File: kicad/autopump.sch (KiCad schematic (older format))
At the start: 12 parts, among them P1 HE10-16, P2 CONN_01X03, P3 CONN_01X06, P4 CONN_01X16, SW1 SW_PUSH, SW2 SW_PUSH

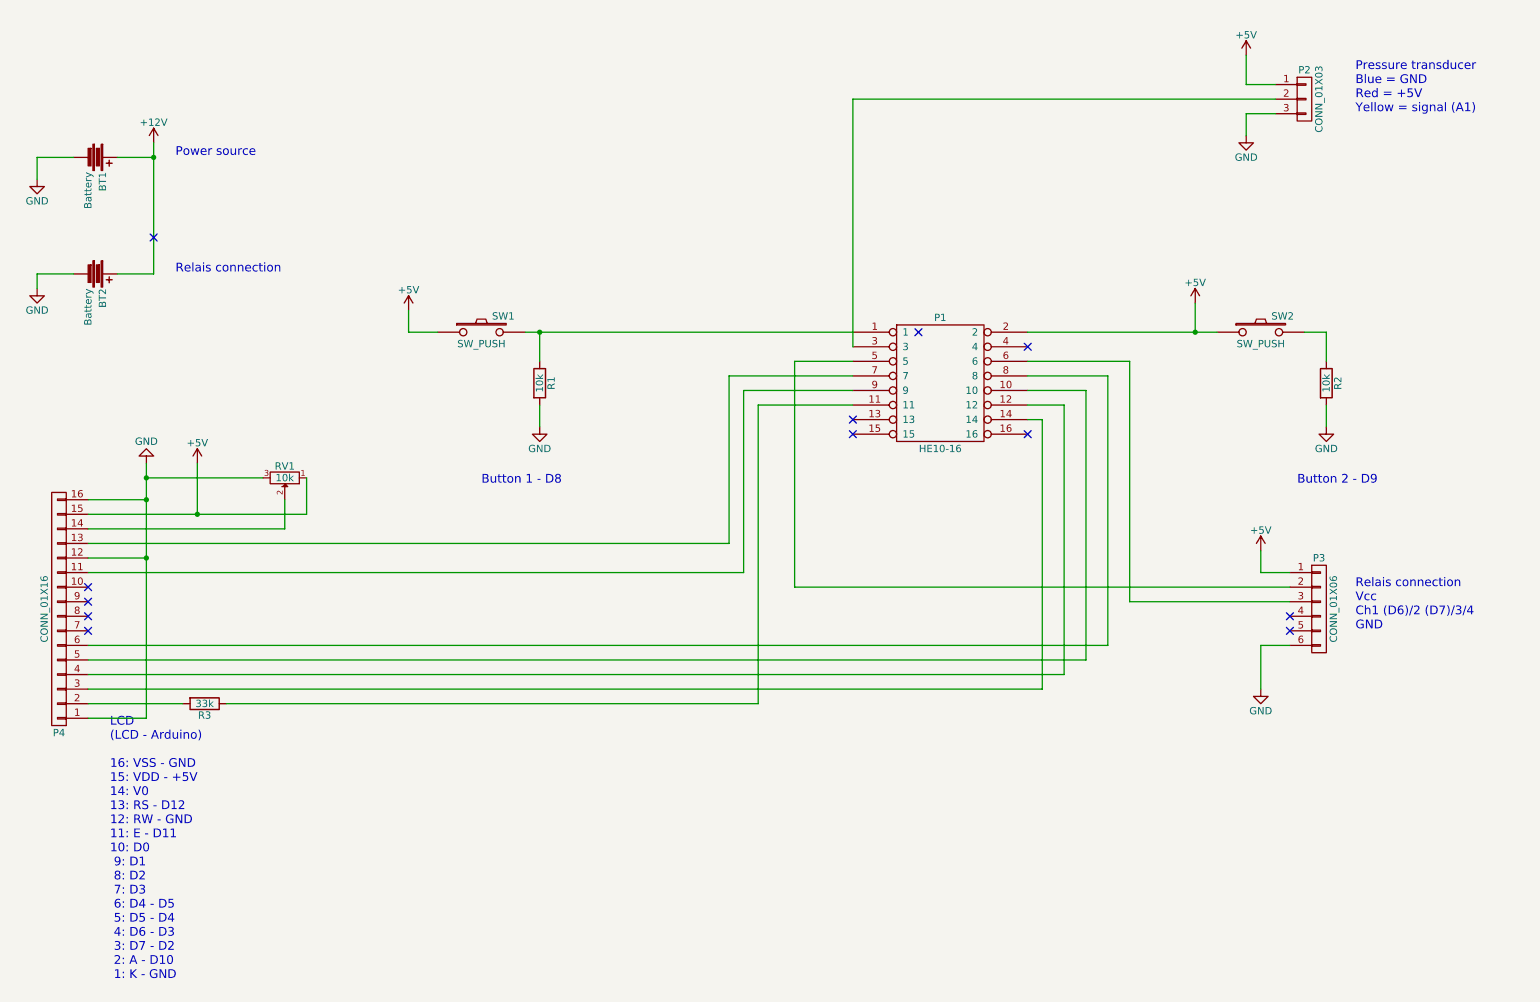
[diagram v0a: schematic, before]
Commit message: More work on the PCB. - make use of the and Arduino shield (http://www.thingiverse.com/thing:9630) library. - reorganize layouts of components - changed the track width and clearances a bit wider - added my name, URL and OSHW logo to PCB
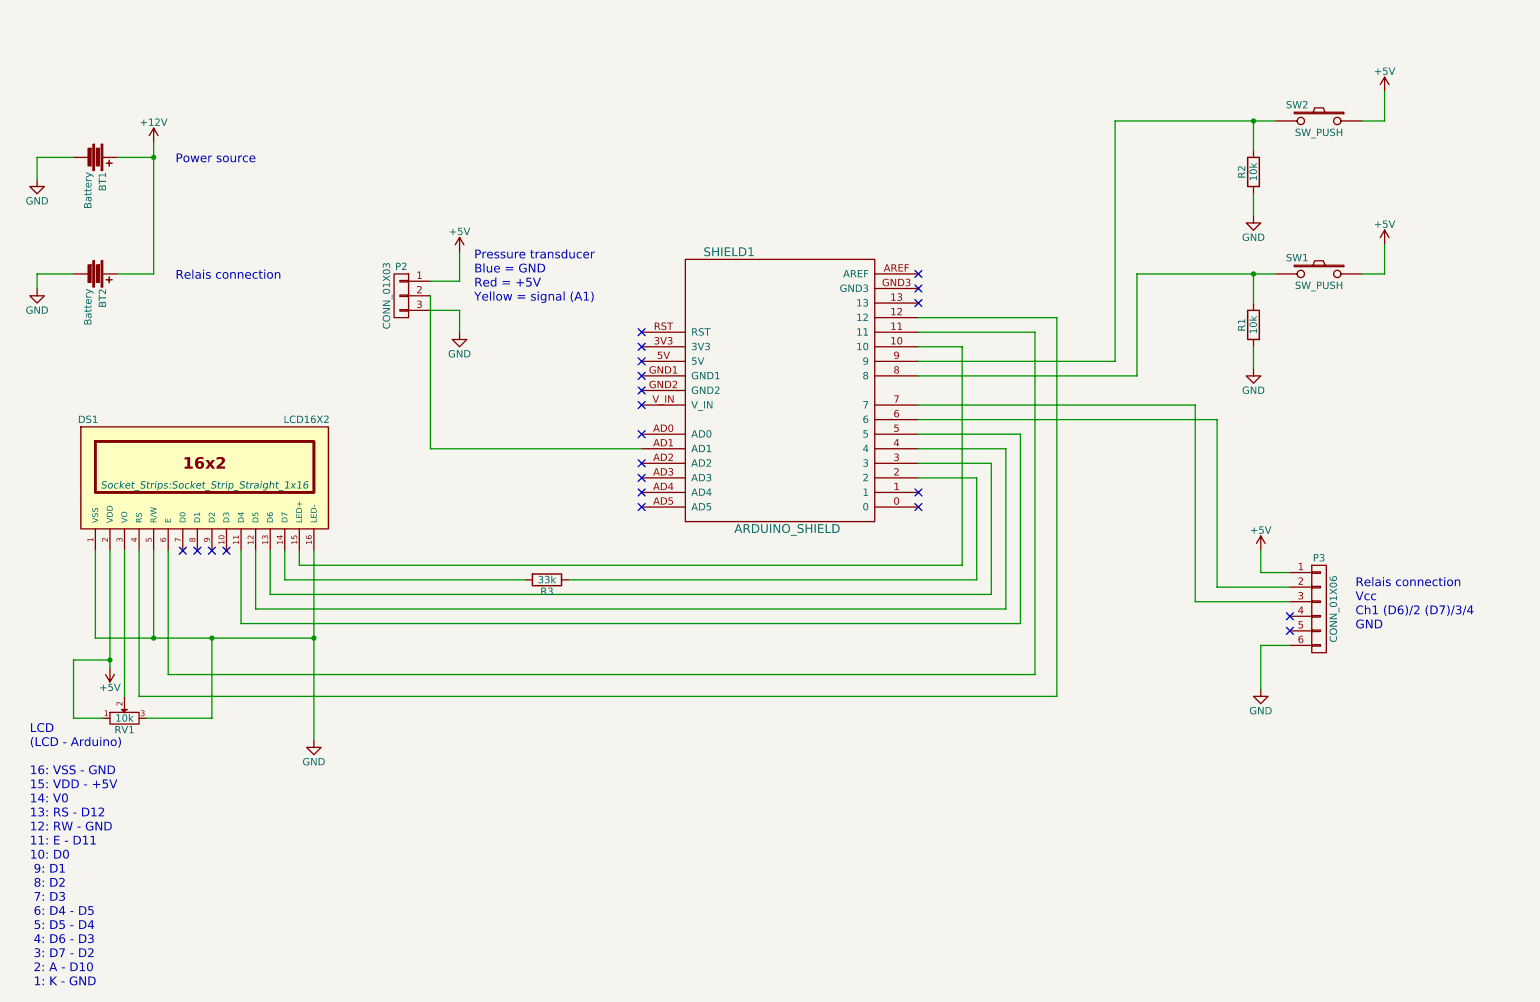
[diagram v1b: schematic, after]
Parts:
- removed P1: HE10-16, Socket_Strips:Socket_Strip_Straight_2x08, symbol HE10-16
- removed P4: CONN_01X16, Pin_Headers:Pin_Header_Straight_1x16, symbol CONN_01X16
- added DS1: LCD16X2, Socket_Strips:Socket_Strip_Straight_1x16, symbol LCD16X2
- added SHIELD1: ARDUINO_SHIELD, arduino_shields:ARDUINO SHIELD, symbol ARDUINO_SHIELD
- BT1, BT2: footprint Wire_Pads:SolderWirePad_2x_1-2mmDrill -> Socket_Strips:Socket_Strip_Straight_1x02
- P2: footprint Pin_Headers:Pin_Header_Straight_1x03 -> Socket_Strips:Socket_Strip_Straight_1x03
- P3: footprint Pin_Headers:Pin_Header_Straight_1x06 -> Socket_Strips:Socket_Strip_Straight_1x06
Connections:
- net +5V: now also DS1.2 (VDD)
- net GND: now also DS1.1 (VSS), DS1.16 (LED-), DS1.5 (R/W)
- net at R1.1, SW1.2: now also SHIELD1.8
- net at R2.1, SW2.2: now also SHIELD1.9
- net at R3.1: now also SHIELD1.2
- net at P2.2 (P2): now also SHIELD1.AD1
- net at P3.2 (P2): now also SHIELD1.6
- net at P3.3 (P3): now also SHIELD1.7
- net at RV1.2: now also DS1.3 (VO)
- net at R3.2: now also DS1.14 (D7)
- new net: DS1.15 (LED+), SHIELD1.10
- new net: DS1.6 (E), SHIELD1.11
- new net: DS1.4 (RS), SHIELD1.12
- new net: DS1.13 (D6), SHIELD1.3
- new net: DS1.12 (D5), SHIELD1.4
- new net: DS1.11 (D4), SHIELD1.5
- no-connect marks 12 -> 22
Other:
- note removed: "Button 1 - D8"
- note removed: "Button 2 - D9"
- moved on the sheet: P2, R1, R2, R3, RV1, SW1, SW2

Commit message: More work on the schema and PCB   - fixed and reorganized the power supply in the schema   - changed the footprints to be more suitable   - reorgnized the footprints slightly on the PCB for better layout and connectivity
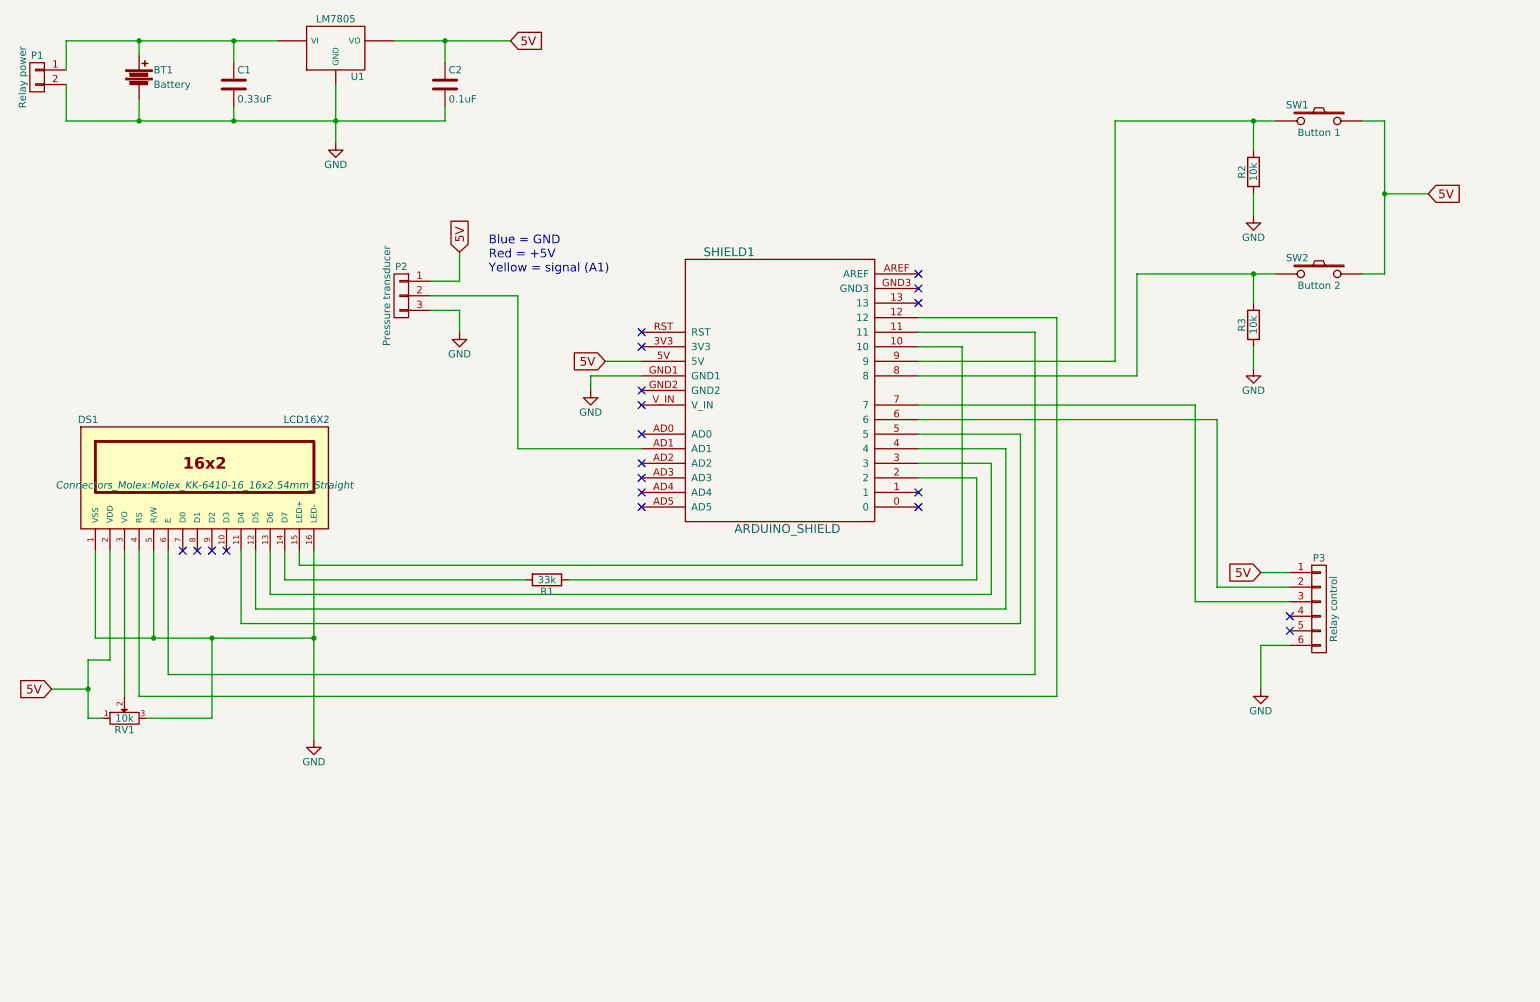
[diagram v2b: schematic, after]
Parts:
- removed BT2: Battery, Socket_Strips:Socket_Strip_Straight_1x02, symbol Battery
- added C1: 0.33uF, Capacitors_ThroughHole:C_Radial_D8_L11.5_P3.5, symbol C
- added C2: 0.1uF, Capacitors_ThroughHole:C_Radial_D8_L11.5_P3.5, symbol C
- added P1: Relay power, Connect:PINHEAD1-2, symbol CONN_01X02
- added U1: LM7805, TO_SOT_Packages_THT:SOT126_SOT32_Housing_Horizontal, symbol LM7805
- BT1: footprint Socket_Strips:Socket_Strip_Straight_1x02 -> Connect:PINHEAD1-2
- DS1: footprint Socket_Strips:Socket_Strip_Straight_1x16 -> Connectors_Molex:Molex_KK-6410-16_16x2.54mm_Straight
- P2: value CONN_01X03 -> Pressure transducer
- P3: value CONN_01X06 -> Relay control; footprint Socket_Strips:Socket_Strip_Straight_1x06 -> Connect:PINHEAD1-6
- RV1: footprint Potentiometers:Potentiometer_Trimmer-Piher_PT15-V17-5_horizontal -> Potentiometers:Potentiometer_Trimmer-Piher_PT15-V12-5_horizontal
- SW1: renamed from SW2; value SW_PUSH -> Button 1; footprint Buttons_Switches_ThroughHole:SW_DIP_x1_Slide -> Connect:PINHEAD1-2
- SW2: renamed from SW1; value SW_PUSH -> Button 2; footprint Buttons_Switches_ThroughHole:SW_DIP_x1_Slide -> Connect:PINHEAD1-2
- renumbered R3 to R1, R1 to R3
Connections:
- net +5V is gone; now on net 5V: DS1.2 (VDD), P2.1 (P1), P3.1 (P1), RV1.1, SW1.1, SW2.1
- net GND: now also SHIELD1.GND1, C1.2, C2.2, P1.2 (P2), U1.GND
- net 5V: now reaches SHIELD1.5V
- net 5V: now also C2.1, U1.VO
- net +12V: no longer names the net of BT1.1
- net +12V: now also C1.1, P1.1 (P1), U1.VI
- no-connect marks 22 -> 20
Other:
- note added: "Blue = GND\nRed = +5V\nYellow = signal (A1)"
- note removed: "LCD\n(LCD - Arduino)\n\n16: VSS - GND\n15: VDD - +5V\n14: V0\n13: RS - D12\n12: RW - GND\n11: E - D11\n10: D0\n 9: D1\n 8: D2\n 7: D3\n 6: D4 - D5\n 5: D5 - D4\n 4: D6 - D3\n 3: D7 - D2\n 2: A - D10\n 1: K - GND"
- note removed: "Power source"
- note removed: "Pressure transducer\nBlue = GND\nRed = +5V\nYellow = signal (A1)"
- note removed: "Relais connection"
- note removed: "Relais connection\nVcc\nCh1 (D6)/2 (D7)/3/4\nGND"
- moved on the sheet: BT1

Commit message: Removed some unneeded kicad files from github Replaced LM7805 component by the LM7805CT component Added +12V symbol to schema so the PCB design rules work again. Issue #4 Reorganized the board a bit to get a better layout. No vias needed and all power traces on the front Relocated the OSHW logo and text box to a more suitable location Resolved issue #5: connections to the side and using a Phoenix terminal block for the pressure transducer Added a printout of the PCB rendering to github Renamed autopump.pdf to autopump_pcb.pdf
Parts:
- removed U1: LM7805, TO_SOT_Packages_THT:SOT126_SOT32_Housing_Horizontal, symbol LM7805
- added U1: LM7805CT, TO-220, symbol LM7805CT
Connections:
- net 5V: now also U1.3 (OUT)
- net GND: now also U1.2 (GND)
- net +12V: now reaches BT1.1, C1.1, P1.1 (P1)
- net +12V: now also U1.1 (IN)
- net at P3.2 (P2): now also SHIELD1.7; no longer SHIELD1.6
- net at P3.3 (P3): now also SHIELD1.6; no longer SHIELD1.7
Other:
- moved on the sheet: BT1, C1, C2, P1
